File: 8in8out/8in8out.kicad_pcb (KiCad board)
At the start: 2 copper layers, 58 parts, among them IC1 ATTINY48-A, J1 RJ45, J2 RJ45, J3 CONN_6, K110 G5T-1-12VDC, K120 G5T-1-12VDC, K130 G5T-1-12VDC, K140 G5T-1-12VDC, K150 G5T-1-12VDC, K160 G5T-1-12VDC, K170 G5T-1-12VDC, K180 G5T-1-12VDC, P1 CONN_5, P100 CONN_2, P101 CONN_2, P102 CONN_2, P103 CONN_2, P105 CONN_2, P106 CONN_2, P110 CONN_2, P120 CONN_2, P130 CONN_2, P140 CONN_2, P150 CONN_2, P160 CONN_2, P170 CONN_2, P180 CONN_2, P2 CONN_5, P3 CONN_10X2, P4 CONN_2, U1 7805, U10 OPTO-TRANSISTOR, U2 ULN2803, U20 OPTO-TRANSISTOR, U30 OPTO-TRANSISTOR, U40 OPTO-TRANSISTOR, U50 OPTO-TRANSISTOR, U60 OPTO-TRANSISTOR, U70 OPTO-TRANSISTOR, U80 OPTO-TRANSISTOR

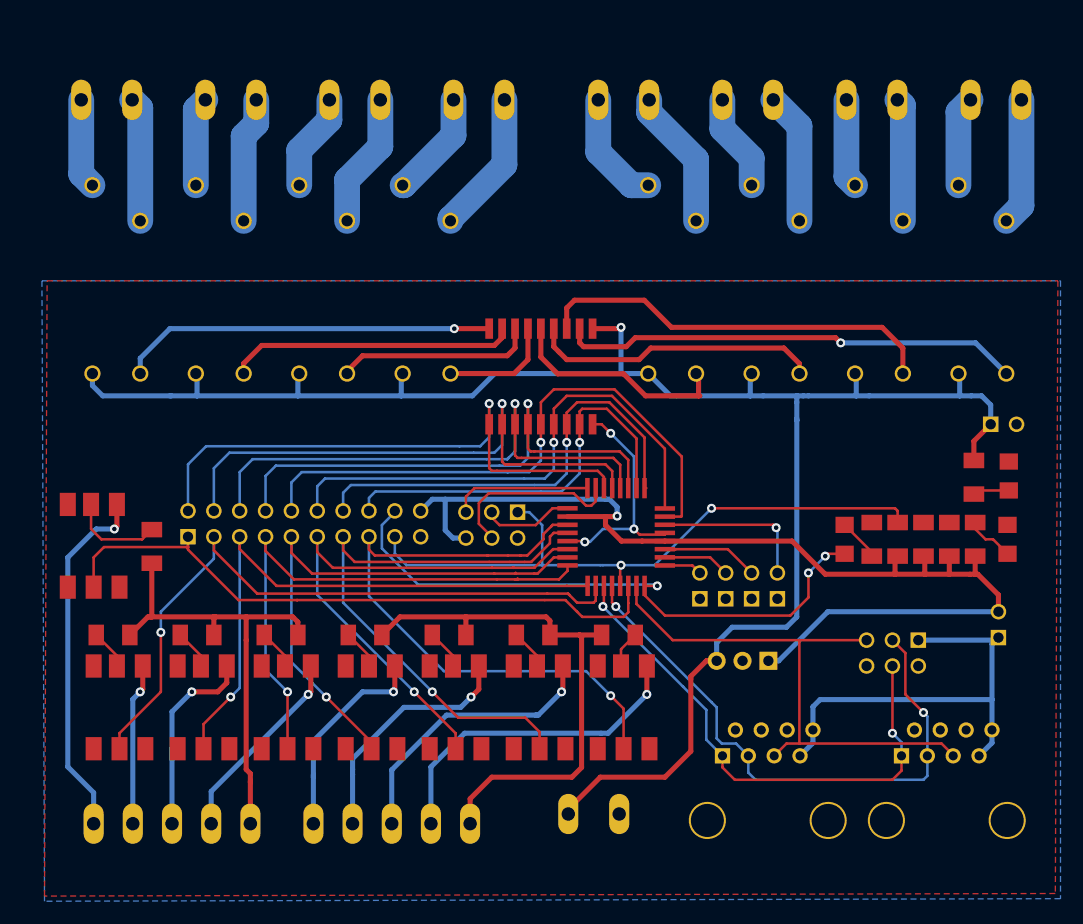
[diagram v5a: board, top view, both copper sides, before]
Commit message: reprise plan de masse pour distances de s?cu ajout r?sistances de pullup i2c doublement pistes de puissance 230VAC
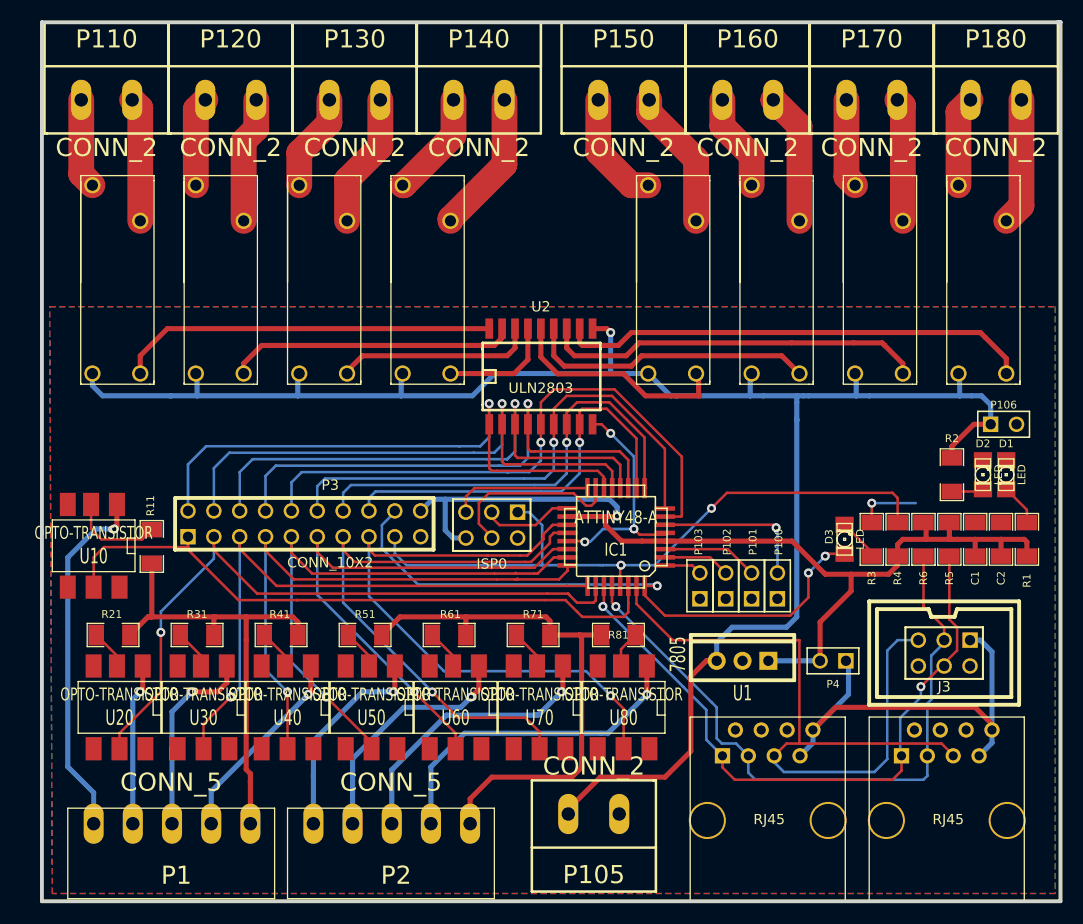
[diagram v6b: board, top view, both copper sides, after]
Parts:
- added R5: 10KR, SM1206, F.Cu at (270.8, 121.9)
- added R6: 10KR, SM1206, F.Cu at (268.2, 121.9)
- R1, R11, R21, R3, R31, R41, R51, R61, R71, R81: value R -> 2KR
- R2: value R -> 4.7KR
- R4: value R -> 10KR
- moved P4 16.6 mm to (259.3, 133.9), turned to 180 degrees
- moved D1 6.35 mm to (276.4, 115.6)
- moved R1 5.08 mm to (278.4, 121.9)
- moved C1 5.08 mm to (273.3, 121.9)
- moved C2 5.08 mm to (275.8, 121.9)
- moved J3 5.08 mm to (270.3, 133.1)
- moved D2 2.54 mm to (274.1, 115.6)
- moved R2 2.17 mm to (271.0, 115.6)
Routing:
- net /INT: track 54.6 -> 74.8 mm
- net SDA: track 51.9 -> 65.1 mm
- net SCL: track 57.5 -> 65.9 mm, vias 2 -> 1
- net GND: track 23.0 -> 29.2 mm, vias 3 -> 4
- net +5V: track 107.7 -> 101.7 mm
- net R6: track 39.8 -> 37.6 mm
- net RESET: track 64.0 -> 66.0 mm
- net R7: track 45.5 -> 46.5 mm, vias 1 -> 0
- net 5V_EXT: track 43.6 -> 44.6 mm
- net N-0000089: track 4.82 -> 4.12 mm
- net +12V: track 177.5 -> 178.1 mm
- net R0: track 37.2 -> 37.1 mm, vias 1 -> 0
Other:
- board outline added: 100.1 x 86.4 mm

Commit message: Agrandissement pad des contacts relais Alignement composants Ajout logo
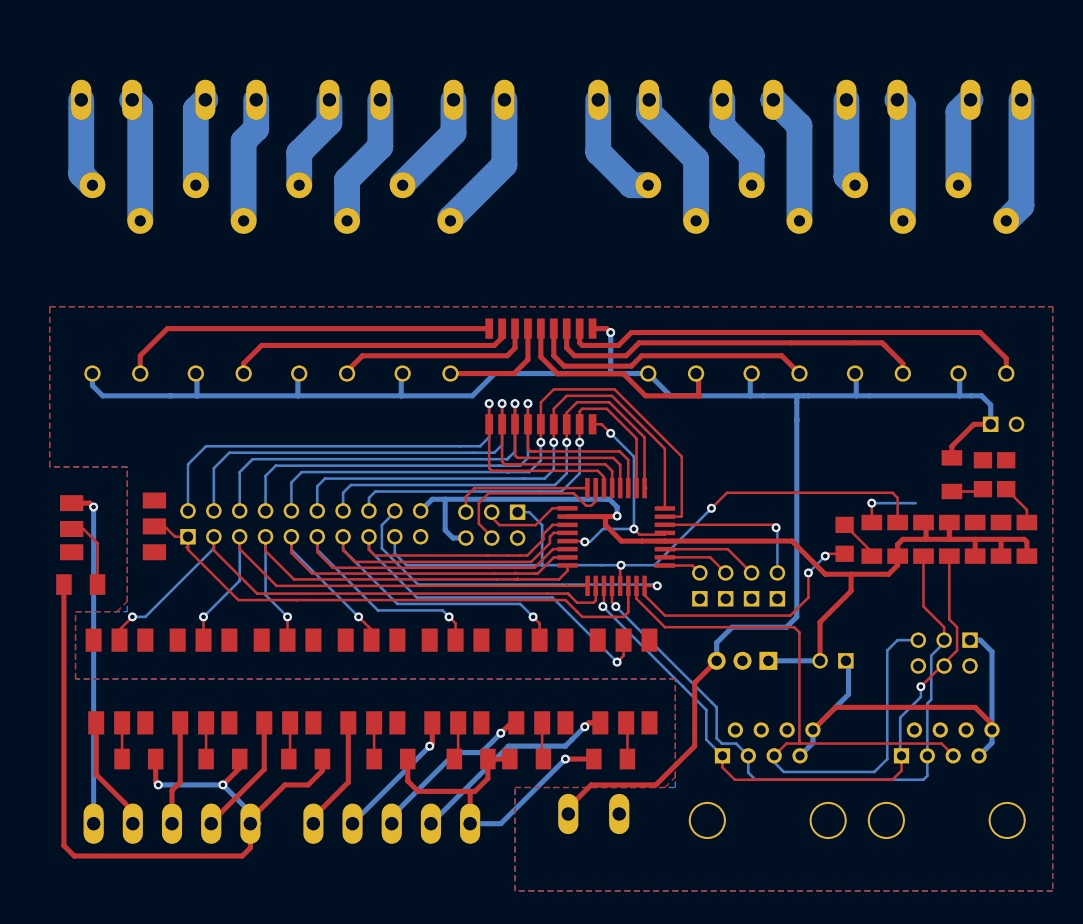
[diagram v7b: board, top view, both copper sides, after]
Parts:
- added logo_xplduino: VAL**, logo_xplduino, F.Cu at (231.4, 94.0)
- added logo_xplduino: VAL**, logo_xplduino, B.Cu at (231.4, 92.7)
- moved R21 12.5 mm to (191.1, 143.5)
- moved R31 12.5 mm to (199.4, 143.5)
- moved R51 12.5 mm to (215.9, 143.5)
- moved R41 12.4 mm to (207.5, 143.5)
- moved R61 12.4 mm to (223.8, 143.5)
- moved R81 12.2 mm to (237.5, 143.5)
- moved R71 12.2 mm to (229.2, 143.5), turned to 180 degrees
- moved R11 7.93 mm to (185.4, 126.4), turned to 180 degrees
- moved U10 2.69 mm to (188.6, 120.7), turned to 270 degrees
- moved U20 2.54 mm to (189.2, 135.9), turned to 0 degrees
- moved U30 2.54 mm to (197.5, 135.9), turned to 0 degrees
- moved U40 2.54 mm to (205.7, 135.9), turned to 0 degrees
- moved U50 2.54 mm to (214.0, 135.9), turned to 0 degrees
- moved U60 2.54 mm to (222.2, 135.9), turned to 0 degrees
- moved U70 2.54 mm to (230.5, 135.9), turned to 0 degrees
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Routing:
- net COM0: track 46.7 -> 75.7 mm, vias 0 -> 2
- net COM1: track 53.4 -> 33.4 mm, vias 0 -> 1
- net IN7: track 32.5 -> 20.7 mm
- net CMD3: track 55.9 -> 44.2 mm
- net CMD4: track 55.3 -> 43.8 mm
- net CMD2: track 59.8 -> 48.5 mm
- net IN6: track 27.9 -> 16.8 mm
- net IN5: track 24.0 -> 13.2 mm
- net CMD1: track 67.8 -> 57.4 mm
- net IN2: track 20.3 -> 10.2 mm, vias 1 -> 0
- net IN4: track 20.8 -> 11.3 mm, vias 1 -> 0
- net CMD0: track 63.0 -> 54.1 mm
- net IN3: track 19.5 -> 12.1 mm, vias 1 -> 0
- net CMD6: track 58.1 -> 50.6 mm
- net CMD5: track 54.1 -> 47.2 mm
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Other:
- board outline removed
